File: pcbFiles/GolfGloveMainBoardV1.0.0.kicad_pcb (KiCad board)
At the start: 4 copper layers, 80 parts, among them J1 USB_C_Receptacle, J11 Conn_01x16_Male, J12 HOST_WAKE, J13 TP4, J14 Conn_01x02, J15 Conn_01x02, J16 Conn_01x02, J17 Conn_01x02, J2 Conn_01x06, J3 USB_C_Receptacle, J4 Conn_01x01, J5 Conn_01x01, J6 Screw_Terminal_01x02, J7 Conn_01x02, J8 Conn_01x02, J9 Conn_01x02, SW1 SW_SPDT, SW2 SW_Push, U1 MCP73831T-2ACI/OT, U2 XC6119N16A7R-G, U3 LSM9DS1TR, U4 CYW20719B1KUMLG, U5 LSM9DS1TR, U7 TPS63001DRCT, Y1 Crystal, Y2 Crystal_GND23

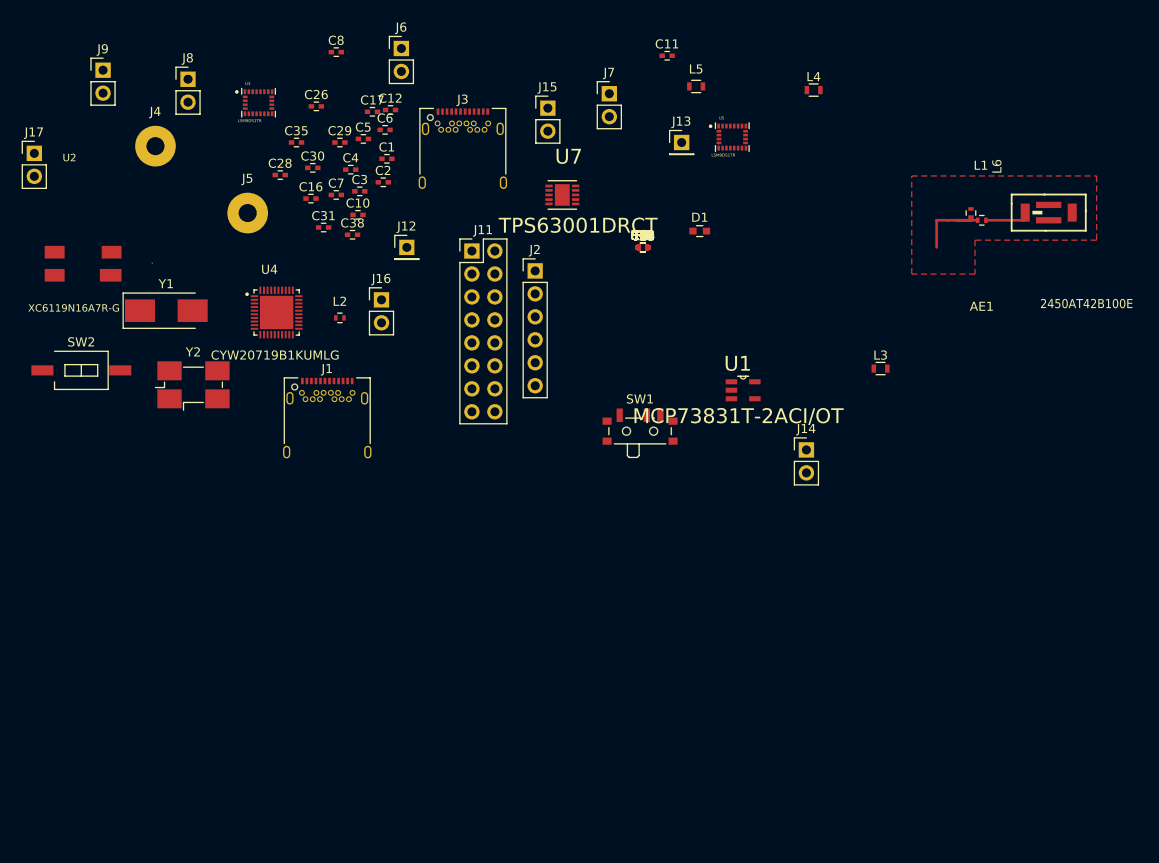
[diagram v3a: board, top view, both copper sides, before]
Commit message: Update Board Files
Updated schematic files, completed REV1.0 of the board design, waiting for review by @willcarroll7
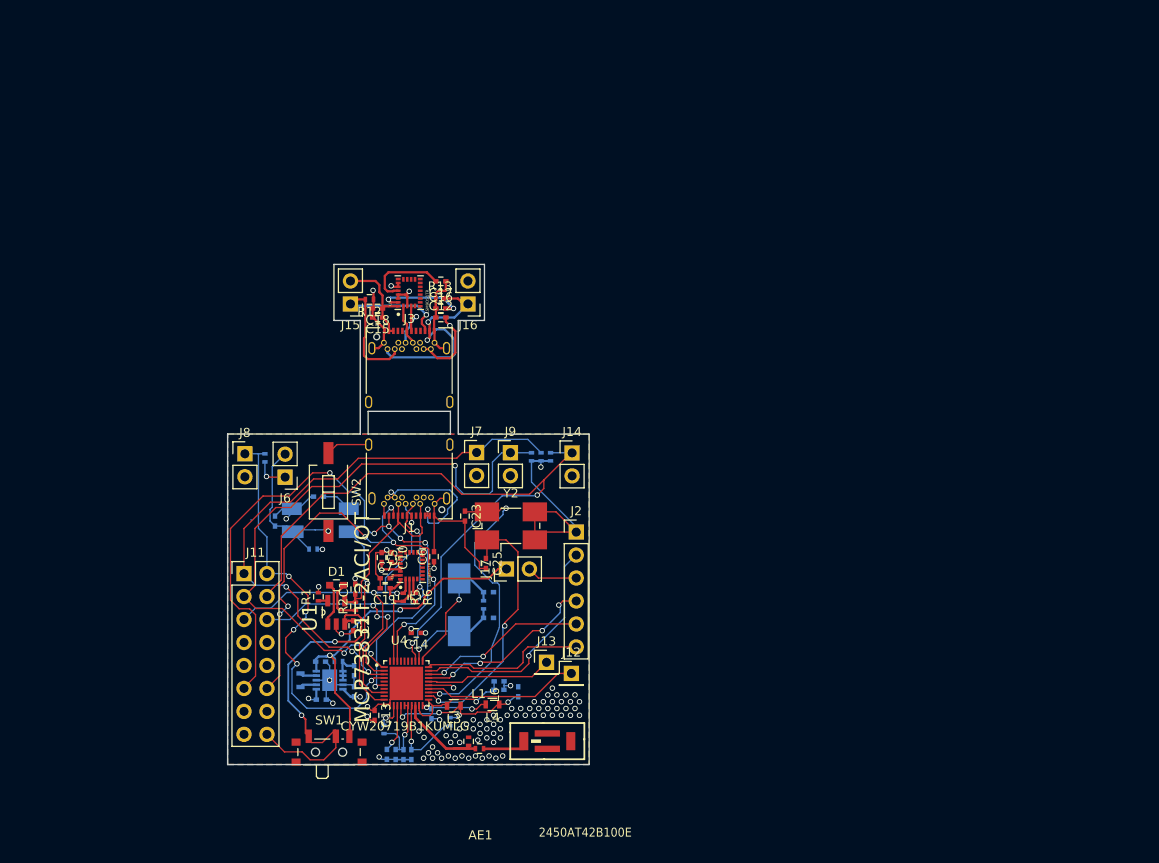
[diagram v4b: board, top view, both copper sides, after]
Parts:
- removed J4, J5: Conn_01x01, Wire_Pads:SolderWirePad_single_2mmDrill
- C22, C26, C28, C29, C3, C30, C31, C32, C33, C35, C36, C37, C38, C4, C8, C9, L2, L5, R10, R11, R15, R3, R4, R7, R8, R9, U2, U7, Y1: moved to B.Cu
- moved L1 80.6 mm to (130.4, 160.4)
- moved L6 80.6 mm to (129.2, 159.6)
- moved AE1 80.6 mm to (137.9, 159.6)
- moved L5 78.9 mm to (110.6, 152.9), turned to 270 degrees
- moved L4 76.7 mm to (131.9, 155.6), turned to 180 degrees
- moved C26 72.5 mm to (122.9, 161.1), turned to 90 degrees
- moved J17 69.6 mm to (133.4, 140.6), turned to 90 degrees
- moved C29 68.0 mm to (121.2, 161.1), turned to 90 degrees
- moved C11 66.6 mm to (120.0, 142.7), turned to 180 degrees
- moved C30 65.7 mm to (122.0, 161.1), turned to 90 degrees
- moved C8 64.8 mm to (131.4, 146.0)
- moved C28 62.9 mm to (134.7, 154.2), turned to 90 degrees
- moved C22 62.8 mm to (120.2, 161.1), turned to 270 degrees
- moved J9 61.8 mm to (133.9, 127.7)
- moved C37 61.4 mm to (112.9, 155.0)
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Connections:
- C12 pad 1: GND -> USBGND
- C12 pad 2: 3.3v -> USBVCC
- C15 pad 1: 3.3v -> USBVCC
- C15 pad 2: GND -> USBGND
- C16 pad 1: GND -> USBGND
- C17 pad 1: GND -> USBGND
- C18 pad 1: 3.3v -> USBVCC
- C18 pad 2: GND -> USBGND
- J1 pad A10: Net-(J1-PadA10) -> PSensor1
- J1 pad A11: Net-(J1-PadA11) -> PSensor2
- J11 pad 1: PSensor1 -> Sensor1
- J11 pad 10: SCLK -> Net-(J11-Pad10)
- J11 pad 11: Net-(J11-Pad11) -> PSensor2
- J11 pad 13: SDA -> Net-(J11-Pad13)
- J11 pad 15: Net-(J11-Pad15) -> GND
- J11 pad 2: PSensor1 -> Sensor2
- J11 pad 3: Net-(J11-Pad3) -> Sensor3
- J11 pad 4: Net-(J11-Pad4) -> Sensor4
- J11 pad 5: Net-(J11-Pad5) -> SCLK
- J11 pad 6: Net-(J11-Pad6) -> SDA
- J11 pad 8: PSensor1 -> Net-(J11-Pad8)
- J14 pad 1: PSensor1 -> Sensor4
- J15 pad 2: 3.3v -> USBVCC
- J16 pad 1: PSensor1 -> PSensor2
- J16 pad 2: 3.3v -> USBVCC
- J3 pad A1: GND -> USBGND
- J3 pad A11: PSensor1 -> PSensor2
- J3 pad A12: GND -> USBGND
- J3 pad A2: 3.3v -> USBVCC
- J3 pad A3: 3.3v -> USBVCC
- J3 pad A6: SCLK -> SCLK-USB
- J3 pad A7: SDA -> SDA-USB
- J3 pad B1: GND -> USBGND
- J3 pad B11: PSensor1 -> PSensor2
- J3 pad B12: GND -> USBGND
- J3 pad B2: 3.3v -> USBVCC
- J3 pad B3: 3.3v -> USBVCC
- J3 pad B6: SCLK -> SCLK-USB
- J3 pad B7: SDA -> SDA-USB
- J3 pad S1: GND -> USBGND
- J7 pad 1: PSensor1 -> Sensor1
- J8 pad 1: PSensor1 -> Sensor2
- J9 pad 1: PSensor1 -> Sensor3
- R10 pad 2: PSensor1 -> Sensor4
- R12 pad 1: GND -> USBGND
- R13 pad 1: GND -> USBGND
- R13 pad 2: PSensor1 -> PSensor2
- R7 pad 2: PSensor1 -> Sensor1
- R8 pad 2: PSensor1 -> Sensor2
- R9 pad 2: PSensor1 -> Sensor3
- SW1 pad 2: Net-(J5-Pad1) -> Net-(J11-Pad16)
- U4 pad 1: PSensor1 -> Sensor3
- U4 pad 3: PSensor1 -> Sensor1
- U4 pad 33: PSensor1 -> Sensor4
- U4 pad 34: Net-(J11-Pad3) -> Net-(U4-Pad34)
- U4 pad 35: Net-(J11-Pad4) -> Net-(U4-Pad35)
- U4 pad 36: Net-(J11-Pad5) -> Net-(U4-Pad36)
- U4 pad 37: Net-(J11-Pad6) -> Net-(U4-Pad37)
- U4 pad 38: Net-(J11-Pad9) -> PSensor1
- U4 pad 4: PSensor1 -> Sensor2
- U4 pad 40: Net-(J11-Pad7) -> Net-(U4-Pad40)
- U4 pad 5: Net-(J11-Pad15) -> Net-(U4-Pad5)
- U4 pad 6: Net-(J11-Pad16) -> PSensor2
- U4 pad 7: Net-(J11-Pad11) -> Net-(U4-Pad7)
- U4 pad 9: Net-(J11-Pad14) -> Net-(U4-Pad9)
- U5 pad 1: 3.3v -> USBVCC
- U5 pad 19: GND -> USBGND
- U5 pad 2: SCLK -> SCLK-USB
- U5 pad 20: GND -> USBGND
- U5 pad 22: 3.3v -> USBVCC
- U5 pad 23: 3.3v -> USBVCC
- U5 pad 3: 3.3v -> USBVCC
- U5 pad 4: SDA -> SDA-USB
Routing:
- net GND: track 0.00 -> 118.4 mm, vias 0 -> 80
- net PSensor2: track 0.00 -> 95.4 mm, vias 0 -> 8
- net PSensor1: track 0.00 -> 80.6 mm, vias 0 -> 8
- net Sensor4: track 0.00 -> 76.0 mm, vias 0 -> 2
- net Sensor3: track 0.00 -> 67.7 mm, vias 0 -> 3
- net Sensor1: track 0.00 -> 64.2 mm, vias 0 -> 4
- net Sensor2: track 0.00 -> 47.2 mm, vias 0 -> 5
- net SCLK: track 0.00 -> 47.1 mm, vias 0 -> 3
- net 3.3v: track 0.00 -> 45.3 mm, vias 0 -> 11
- net SDA: track 0.00 -> 43.8 mm, vias 0 -> 5
- net BatteryOutBuck: track 0.00 -> 39.5 mm, vias 0 -> 2
- net Net-(C23-Pad1): track 0.00 -> 33.2 mm, vias 0 -> 2
- net Net-(C25-Pad1): track 0.00 -> 29.3 mm, vias 0 -> 2
- net /BT_UART_RTS: track 0.00 -> 26.0 mm, vias 0 -> 1
- net BatteryOutChg: track 0.00 -> 25.4 mm, vias 0 -> 2
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- added copper zone on In2.Cu, net 3.3v
- added copper zone on B.Cu, net GND
- added copper zone on In1.Cu, net GND
- added copper zone on In1.Cu, net USBGND
- added copper zone on In2.Cu, net USBVCC
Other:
- board outline added: 40 x 55.3 mm
- net class Default: trace_width 0.25 -> 0.15
- net class Small added: clearance 0.15, trace_width 0.2, via_dia 0.6, via_drill 0.4
- rule trace_min: 0.2 -> 0.15

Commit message: Update Fills and Outlines
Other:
- net class Default: via_dia 0.6 -> 0.5; via_drill 0.4 -> 0.34
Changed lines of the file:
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@@
-(kicad_pcb (version 4) (host pcbnew 4.0.7)
+(kicad_pcb (version 20171130) (host pcbnew "(5.0.2)-1")
   (general
-    (links 216)
-    (no_connects 3)
-    (area 102.504999 106.804999 142.645001 162.275001)
     (thickness 1.6)
     (drawings 27)
@@
   (layers
     (0 F.Cu signal)
-    (1 In1.Cu signal hide)
-    (2 In2.Cu signal hide)
+    (1 In1.Cu signal)
+    (2 In2.Cu signal)
     (31 B.Cu signal)
     (32 B.Adhes user)
@@
     (segment_width 0.2)
     (edge_width 0.15)
-    (via_size 0.6)
-    (via_drill 0.4)
+    (via_size 0.5)
+    (via_drill 0.34)
     (via_min_size 0.4)
     (via_min_drill 0.3)
@@
     (pad_drill 0.762)
     (pad_to_mask_clearance 0.2)
+    (solder_mask_min_width 0.25)
     (aux_axis_origin 0 0)
     (visible_elements 7FFEFFFF)
@@
       (layerselection 0x00030_80000001)
       (usegerberextensions false)
+      (usegerberattributes false)
+      (usegerberadvancedattributes false)
+      (creategerberjobfile false)
       (excludeedgelayer true)
       (linewidth 0.100000)
@@
       (hpglpennumber 1)
       (hpglpenspeed 20)
-      (hpglpendiameter 15)
-      (hpglpenoverlay 2)
+      (hpglpendiameter 15.000000)
       (psnegative false)
       (psa4output false)
@@
     (clearance 0.15)
     (trace_width 0.15)
-    (via_dia 0.6)
-    (via_drill 0.4)
+    (via_dia 0.5)
+    (via_drill 0.34)
     (uvia_dia 0.3)
     (uvia_drill 0.1)
@@
     (fp_line (start 5.8 2.4) (end 5.8 -2.4) (layer F.CrtYd) (width 0.05))
     (fp_line (start 5.8 -2.4) (end -5.8 -2.4) (layer F.CrtYd) (width 0.05))
-    (fp_text user %R (at 2.575 0 360) (layer F.Fab)
+    (fp_text user %R (at 2.575 0) (layer F.Fab)
       (effects (font (size 0.6 0.6) (thickness 0.15)))
     )
@@
     (fp_line (start 0.3048 -1.5494) (end -0.3048 -1.5494) (layer F.SilkS) (width 0.1524))
     (fp_line (start -0.3048 -1.5494) (end -0.6096 -1.5494) (layer F.SilkS) (width 0.1524))
-    (fp_arc (start 0 -1.5494) (end -0.3048 -1.5494) (angle -180) (layer F.SilkS) (width 0))
+    (fp_arc (start 0 -1.5494) (end -0.3048 -1.5494) (angle -180) (layer F.SilkS) (width 0.1))
     (fp_line (start -0.8636 1.5494) (end 0.8636 1.5494) (layer Dwgs.User) (width 0.1524))
     (fp_line (start 0.8636 1.5494) (end 0.8636 1.1938) (layer Dwgs.User) (width 0.1524))
@@
     (fp_line (start 1.4986 -0.7112) (end 1.4986 -1.1938) (layer Dwgs.User) (width 0.1524))
     (fp_line (start 1.4986 -1.1938) (end 0.8636 -1.1938) (layer Dwgs.User) (width 0.1524))
-    (fp_arc (start 0 -1.5494) (end -0.3048 -1.5494) (angle -180) (layer Dwgs.User) (width 0))
+    (fp_arc (start 0 -1.5494) (end -0.3048 -1.5494) (angle -180) (layer Dwgs.User) (width 0.1))
     (pad 1 smd rect (at -1.2954 -0.9398 90) (size 1.27 0.5588) (layers F.Cu F.Paste F.Mask)
       (net 25 "Net-(D1-Pad1)"))
@@
       (effects (font (size 0.812819 0.812819) (thickness 0.05)) (justify mirror))
     )
-    (fp_line (start 0.15 0) (end 3.45 0) (layer Eco2.User) (width 0))
-    (fp_line (start 3.75 0) (end 7.05 0) (layer Eco2.User) (width 0))
-    (fp_line (start 7.2 0.15) (end 7.2 1.2) (layer Eco2.User) (width 0))
-    (fp_line (start 7.2 1.45) (end 7.2 3.75) (layer Eco2.User) (width 0))
-    (fp_line (start 7.2 4) (end 7.2 5.05) (layer Eco2.User) (width 0))
-    (fp_line (start 7.05 5.2) (end 3.75 5.2) (layer Eco2.User) (width 0))
-    (fp_line (start 3.45 5.2) (end 0.15 5.2) (layer Eco2.User) (width 0))
-    (fp_line (start 0 5.05) (end 0 4) (layer Eco2.User) (width 0))
-    (fp_line (start 0 3.75) (end 0 1.45) (layer Eco2.User) (width 0))
-    (fp_line (start 0 1.2) (end 0 0.15) (layer Eco2.User) (width 0))
-    (fp_line (start 11.25 2.61) (end 11.25 2.67) (layer B.Cu) (width 0))
-    (fp_arc (start 0 3.875) (end 0 3.75) (angle 180) (layer Eco2.User) (width 0))
-    (fp_arc (start 0 1.325) (end 0 1.2) (angle 180) (layer Eco2.User) (width 0))
-    (fp_arc (start 0.0375 0.0375) (end 0.15 0) (angle 126.8) (layer Eco2.User) (width 0))
-    (fp_arc (start 3.6 0) (end 3.75 0) (angle 180) (layer Eco2.User) (width 0))
-    (fp_arc (start 3.6 5.2) (end 3.45 5.2) (angle 180) (layer Eco2.User) (width 0))
-    (fp_arc (start 0.0375 5.1625) (end 0 5.05) (angle 126.8) (layer Eco2.User) (width 0))
-    (fp_arc (start 7.2 3.875) (end 7.2 4) (angle 180) (layer Eco2.User) (width 0))
-    (fp_arc (start 7.2 1.325) (end 7.2 1.45) (angle 180) (layer Eco2.User) (width 0))
-    (fp_arc (start 7.1625 5.1625) (end 7.05 5.2) (angle 126.8) (layer Eco2.User) (width 0))
-    (fp_arc (start 7.1625 0.0375) (end 7.2 0.15) (angle 126.8) (layer Eco2.User) (width 0))
+    (fp_line (start 0.15 0) (end 3.45 0) (layer Eco2.User) (width 0.1))
+    (fp_line (start 3.75 0) (end 7.05 0) (layer Eco2.User) (width 0.1))
+    (fp_line (start 7.2 0.15) (end 7.2 1.2) (layer Eco2.User) (width 0.1))
+    (fp_line (start 7.2 1.45) (end 7.2 3.75) (layer Eco2.User) (width 0.1))
+    (fp_line (start 7.2 4) (end 7.2 5.05) (layer Eco2.User) (width 0.1))
+    (fp_line (start 7.05 5.2) (end 3.75 5.2) (layer Eco2.User) (width 0.1))
+    (fp_line (start 3.45 5.2) (end 0.15 5.2) (layer Eco2.User) (width 0.1))
+    (fp_line (start 0 5.05) (end 0 4) (layer Eco2.User) (width 0.1))
+    (fp_line (start 0 3.75) (end 0 1.45) (layer Eco2.User) (width 0.1))
+    (fp_line (start 0 1.2) (end 0 0.15) (layer Eco2.User) (width 0.1))
+    (fp_line (start 11.25 2.61) (end 11.25 2.67) (layer B.Cu) (width 0.1))
+    (fp_arc (start 0 3.875) (end 0 3.75) (angle 180) (layer Eco2.User) (width 0.1))
+    (fp_arc (start 0 1.325) (end 0 1.2) (angle 180) (layer Eco2.User) (width 0.1))
+    (fp_arc (start 0.0375 0.0375) (end 0.15 0) (angle 126.8) (layer Eco2.User) (width 0.1))
+    (fp_arc (start 3.6 0) (end 3.75 0) (angle 180) (layer Eco2.User) (width 0.1))
+    (fp_arc (start 3.6 5.2) (end 3.45 5.2) (angle 180) (layer Eco2.User) (width 0.1))
+    (fp_arc (start 0.0375 5.1625) (end 0 5.05) (angle 126.8) (layer Eco2.User) (width 0.1))
+    (fp_arc (start 7.2 3.875) (end 7.2 4) (angle 180) (layer Eco2.User) (width 0.1))
+    (fp_arc (start 7.2 1.325) (end 7.2 1.45) (angle 180) (layer Eco2.User) (width 0.1))
+    (fp_arc (start 7.1625 5.1625) (end 7.05 5.2) (angle 126.8) (layer Eco2.User) (width 0.1))
+    (fp_arc (start 7.1625 0.0375) (end 7.2 0.15) (angle 126.8) (layer Eco2.User) (width 0.1))
     (pad 2 smd rect (at 0.45 3.87 180) (size 2.2 1.4) (layers B.Cu B.Paste B.Mask)
       (net 5 "Net-(C3-Pad1)"))
@@
     (fp_line (start -1.5748 -1.5748) (end 1.5748 -1.5748) (layer B.SilkS) (width 0.1524))
     (fp_line (start 1.5748 1.5748) (end -1.5748 1.5748) (layer B.SilkS) (width 0.1524))
-    (fp_line (start -1.5748 -1.5748) (end 1.5748 -1.5748) (layer Dwgs.User) (width 0))
-    (fp_line (start 1.5748 -1.5748) (end 1.5748 1.5748) (layer Dwgs.User) (width 0))
-    (fp_line (start 1.5748 1.5748) (end 0.3048 1.5748) (layer Dwgs.User) (width 0))
-    (fp_line (start 0.3048 1.5748) (end -0.3048 1.5748) (layer Dwgs.User) (width 0))
-    (fp_line (start -0.3048 1.5748) (end -1.5748 1.5748) (layer Dwgs.User) (width 0))
-    (fp_line (start -1.5748 1.5748) (end -1.5748 -1.5748) (layer Dwgs.User) (width 0))
-    (fp_arc (start 0 1.5748) (end -0.3048 1.5748) (angle 180) (layer Dwgs.User) (width 0))
+    (fp_line (start -1.5748 -1.5748) (end 1.5748 -1.5748) (layer Dwgs.User) (width 0.1))
+    (fp_line (start 1.5748 -1.5748) (end 1.5748 1.5748) (layer Dwgs.User) (width 0.1))
+    (fp_line (start 1.5748 1.5748) (end 0.3048 1.5748) (layer Dwgs.User) (width 0.1))
+    (fp_line (start 0.3048 1.5748) (end -0.3048 1.5748) (layer Dwgs.User) (width 0.1))
+    (fp_line (start -0.3048 1.5748) (end -1.5748 1.5748) (layer Dwgs.User) (width 0.1))
+    (fp_line (start -1.5748 1.5748) (end -1.5748 -1.5748) (layer Dwgs.User) (width 0.1))
+    (fp_arc (start 0 1.5748) (end -0.3048 1.5748) (angle 180) (layer Dwgs.User) (width 0.1))
     (pad 1 smd rect (at -1.4732 0.9906) (size 0.8128 0.3048) (layers B.Cu B.Paste B.Mask)
       (net 7 3.3v))
@@
     (polygon
       (pts
-        (xy 142.57 125.65) (xy 142.57 160.65) (xy 102.58 160.65) (xy 102.58 125.66)
+        (xy 142.57 125.65) (xy 142.55 162.25) (xy 102.6 162.2) (xy 102.58 125.66)
       )
     )
@@
     (polygon
       (pts
-        (xy 142.57 125.65) (xy 142.57 160.65) (xy 102.57 160.65) (xy 102.57 125.65)
+        (xy 142.57 125.65) (xy 142.5 162.25) (xy 102.55 162.25) (xy 102.57 125.65)
       )
     )
